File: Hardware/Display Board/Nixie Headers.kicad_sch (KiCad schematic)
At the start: 2 parts, among them J26 Conn_02x03_Odd_Even, J27 Conn_02x03_Odd_Even

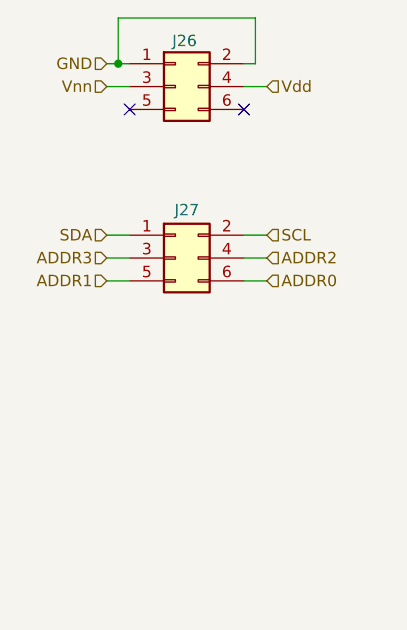
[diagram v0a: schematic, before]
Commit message: Updated Display Board to V2 Nixies
The Antenna holder needs to be redesigned. Lots of silkscreen errors to fix.
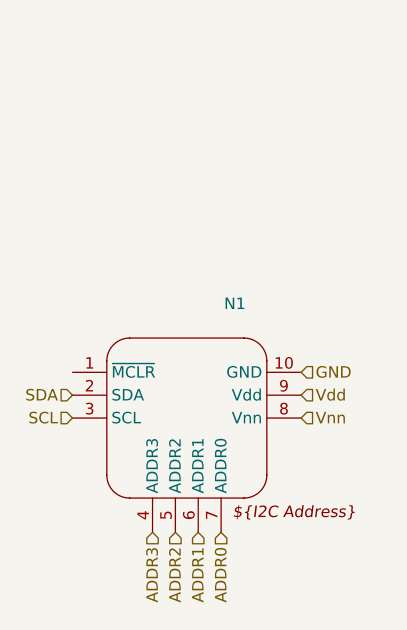
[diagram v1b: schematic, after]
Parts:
- removed J26, J27: Conn_02x03_Odd_Even, Connector_PinSocket_2.54mm:PinSocket_2x03_P2.54mm_Vertical, symbol Connector_Generic:Conn_02x03_Odd_Even
- added N1: ~, Nixie:Nixie Driver V2, symbol Nixie:Nixie_Driver
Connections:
- net ADDR0: now also N1.7 (ADDR0)
- net ADDR1: now also N1.6 (ADDR1)
- net ADDR2: now also N1.5 (ADDR2)
- net ADDR3: now also N1.4 (ADDR3)
- net GND: now also N1.10 (GND)
- net SCL: now also N1.3 (SCL)
- net SDA: now also N1.2 (SDA)
- net Vdd: now also N1.9 (Vdd)
- net Vnn: now also N1.8 (Vnn)
- no-connect marks 2 -> 0
